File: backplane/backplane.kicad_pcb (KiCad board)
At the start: 2 copper layers, 150 x 150 mm, 16 parts

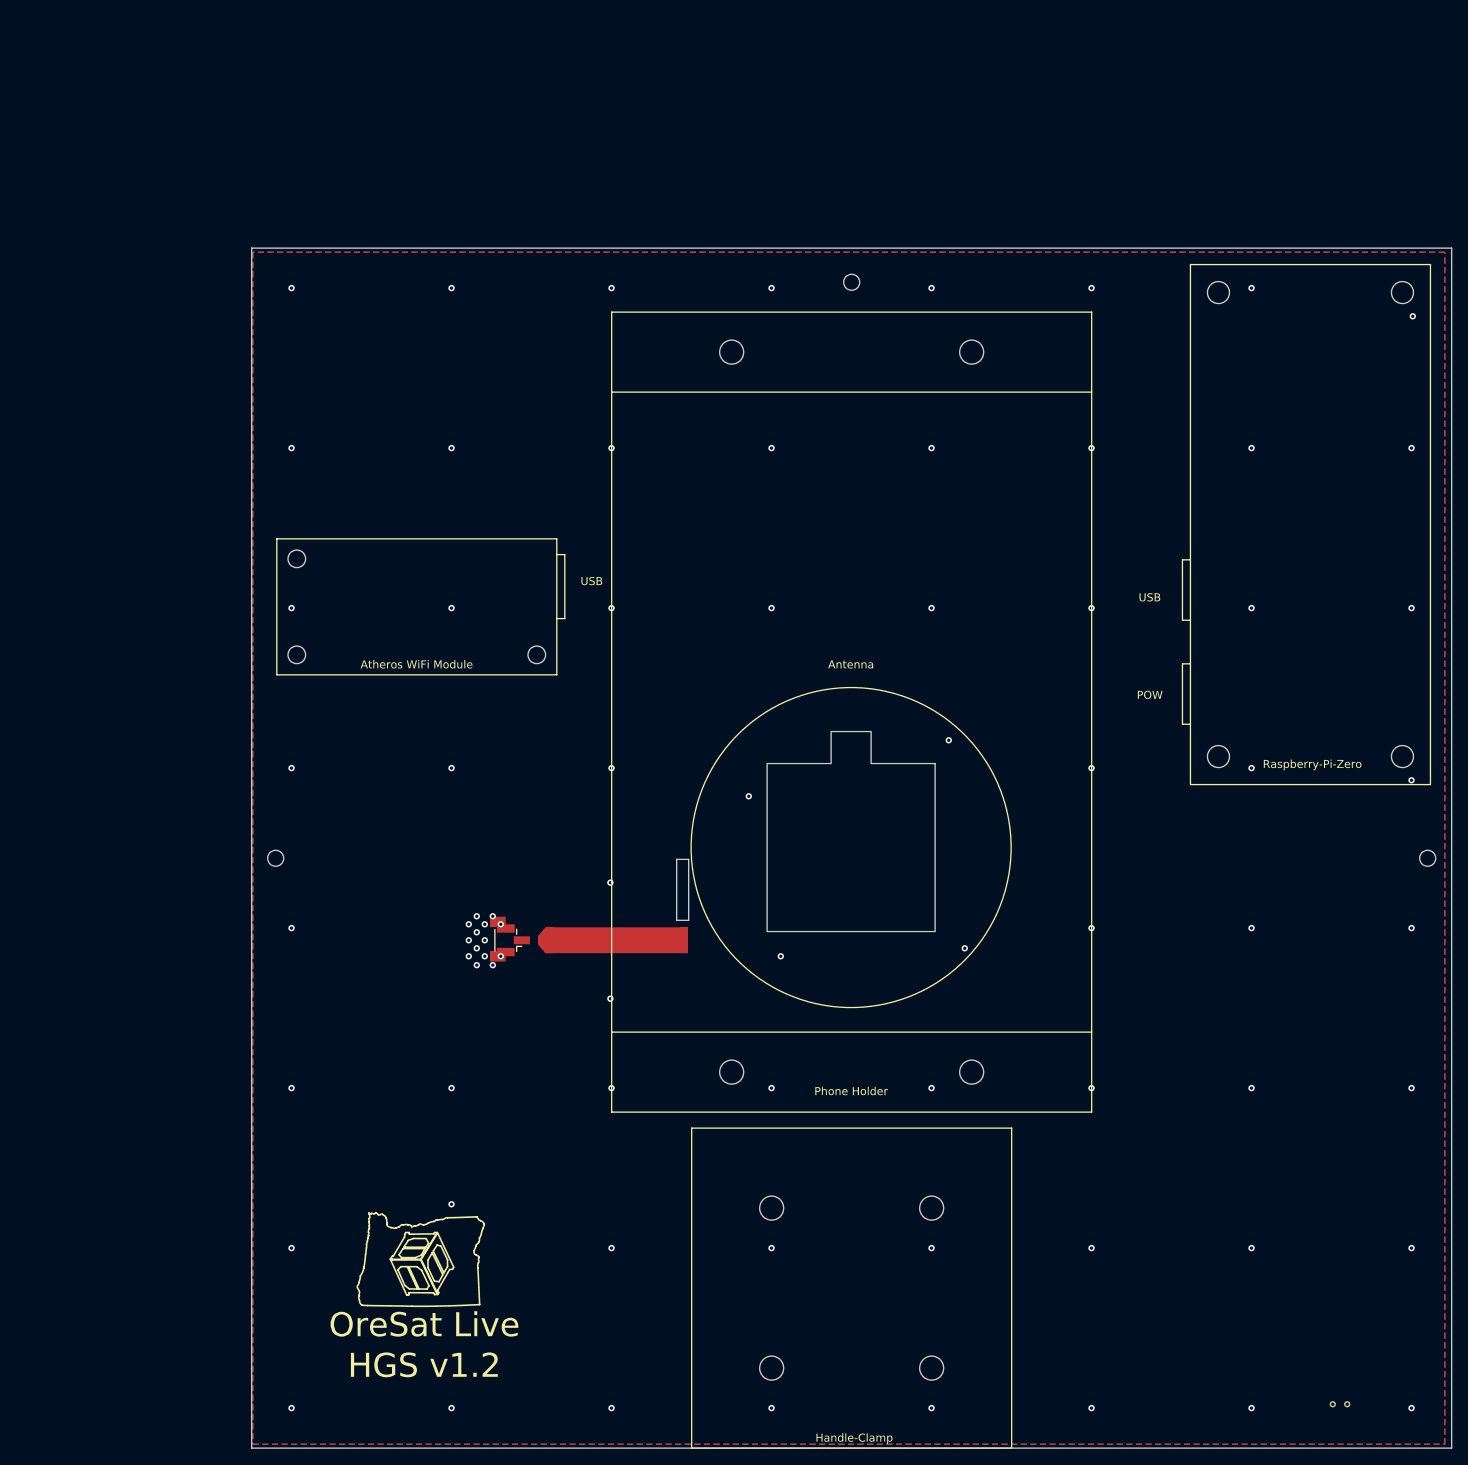
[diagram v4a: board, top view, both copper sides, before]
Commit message: Adding major final changes for transformer strip
Moved transformer parts closer to antenna by 1mm
Transformer microstrip reverted to original intended size
Added footprint for 0402 capacitor to replace gap between U.FL and strip
Modified U.FL footprint pads to be "solid" to allow for copper fill to
   connect to the GND pads
Phone Clamp and Handle mount holes changed to 4.5mm
Fixed README text hyperlink for footprint dimension references
Removed unused/blank footprints in Kicad library
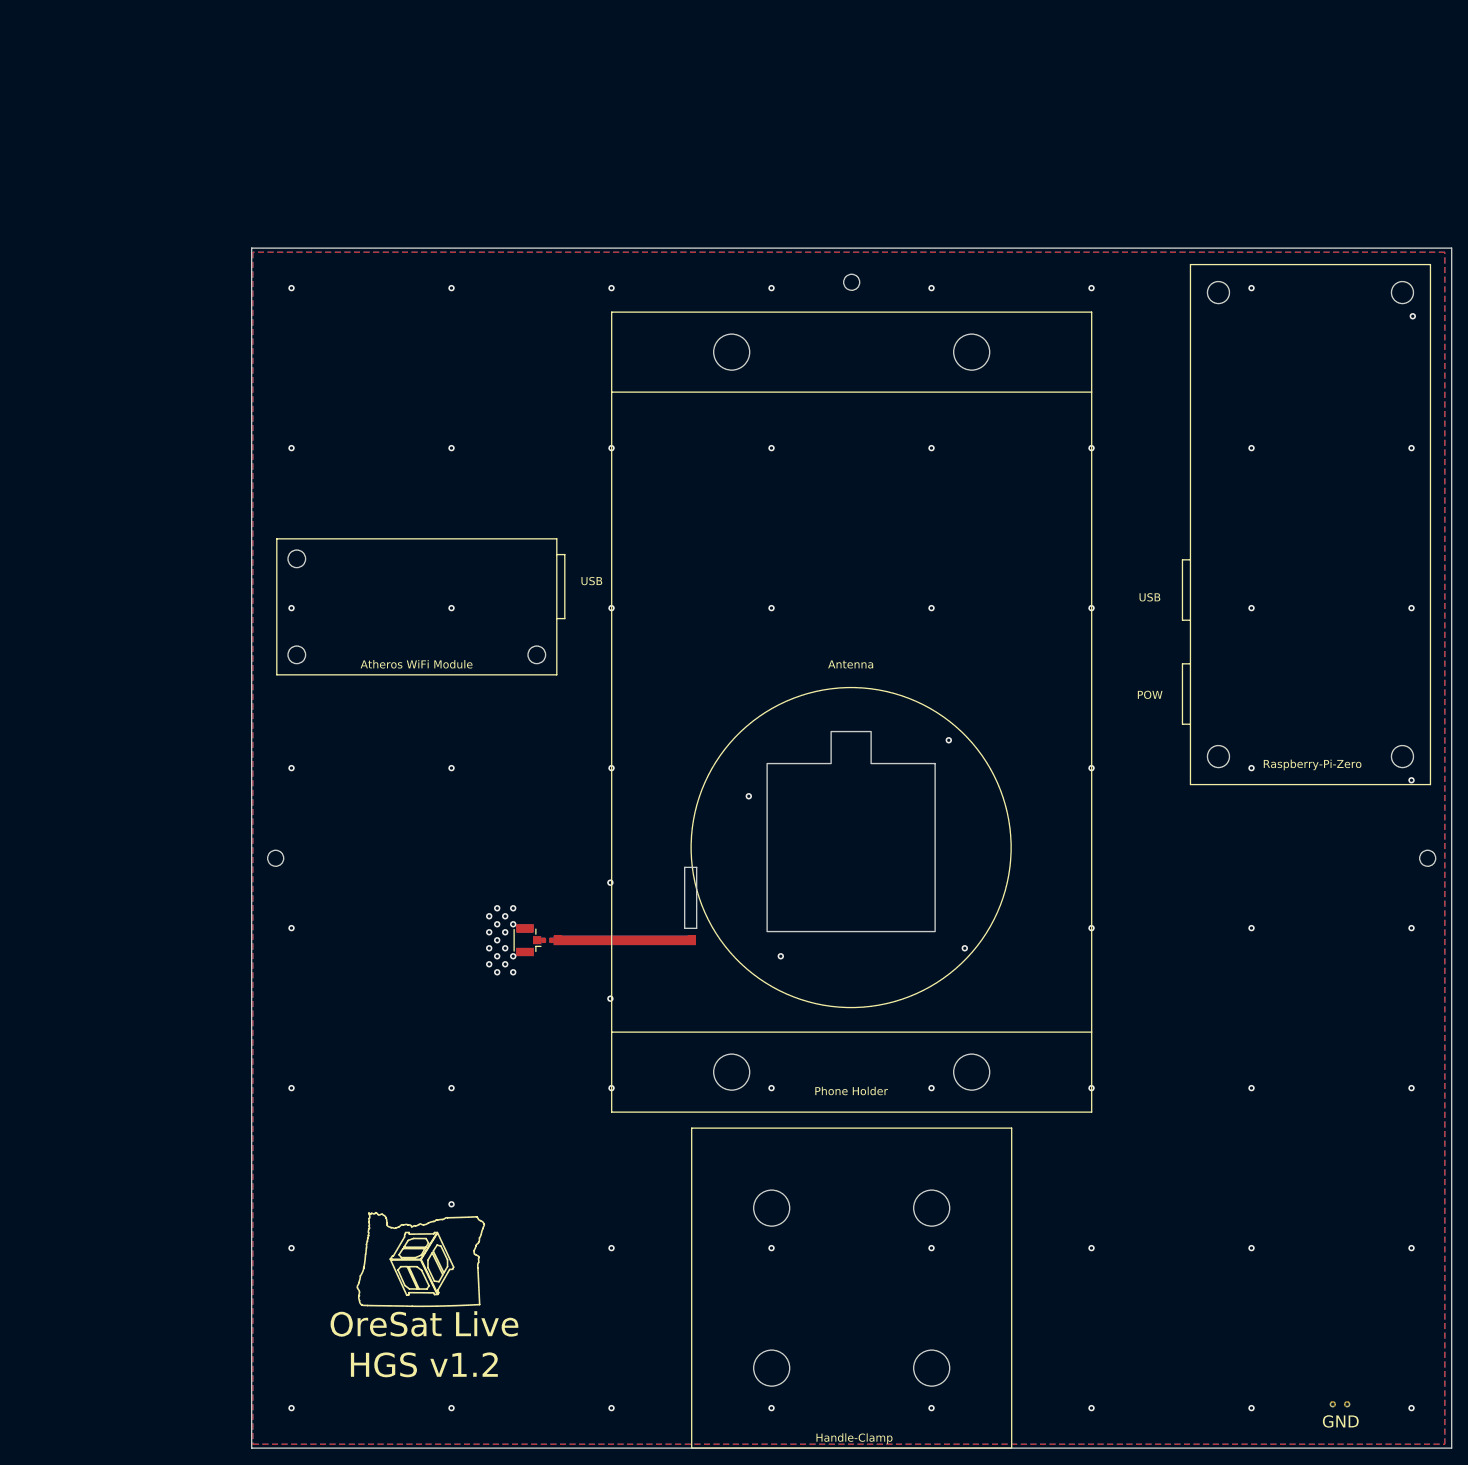
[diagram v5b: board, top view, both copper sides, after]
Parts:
- added REF**: C_0402_1005Metric, DxWiFi:C_0402_1005Metric, F.Cu at (59.9, 117.0)
- moved REF** 2.40 mm to (57.5, 117.0)
- moved REF** 1.41 mm to (79.8, 111.7)
- moved REF** 1.00 mm to (63.0, 117.0)
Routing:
- net Net-(L1-Pad1): vias 78 -> 81
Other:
- board text added: "GND"

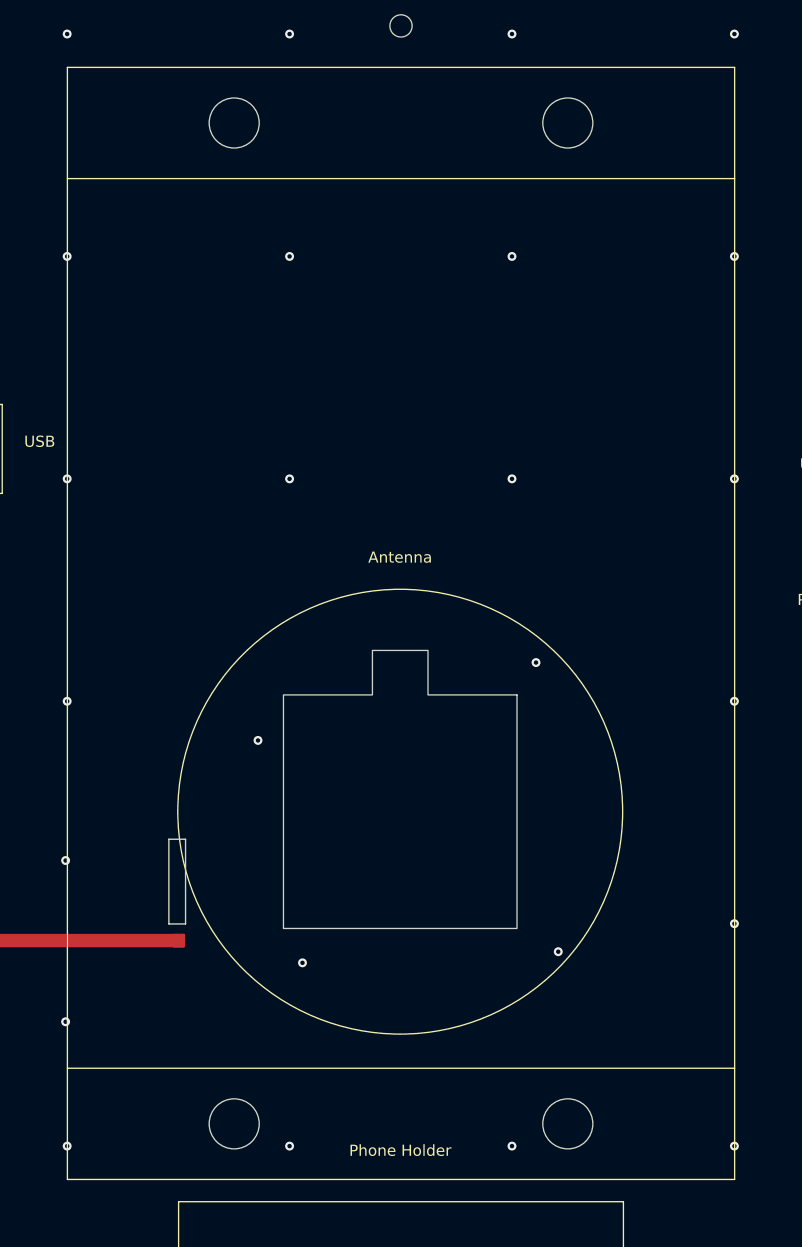
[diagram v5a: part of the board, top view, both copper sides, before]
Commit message: Update Phone Holder footprint to new design
Holes are now 50mm apart horizontally and 90mm vertically
Fixed hyperlinking text for README
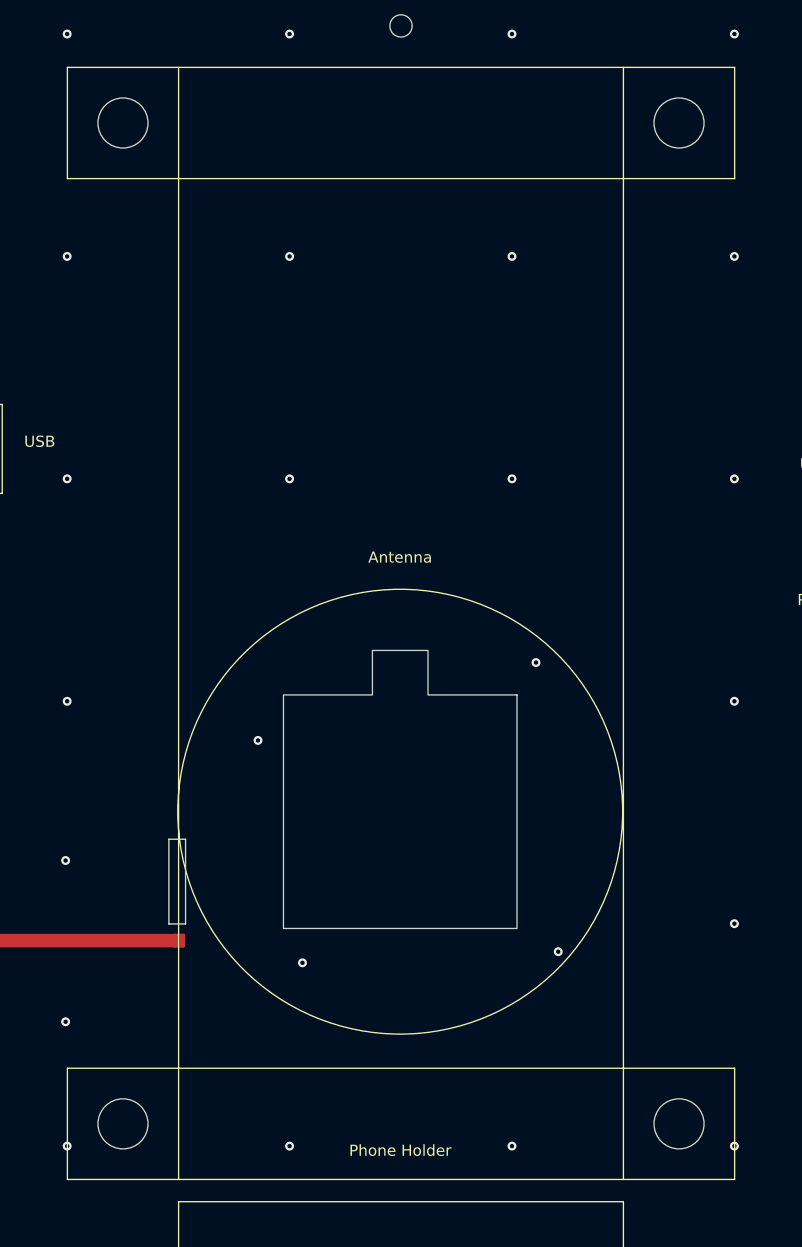
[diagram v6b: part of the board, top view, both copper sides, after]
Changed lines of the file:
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@@
     (add_net "Net-(L1-Pad1)")
+  )
+  (module DxWiFi:Phone-Holder (layer F.Cu)
+    (at 67.86 138.48)
+    (fp_text reference "Phone Holder" (at 29.93 -2.59) (layer F.SilkS)
+      (effects (font (size 1 1) (thickness 0.15)))
+    )
+    (fp_text value Phone-Holder (at 30.48 -5.13) (layer B.SilkS) hide
+      (effects (font (size 1 1) (thickness 0.15)))
+    )
+    (fp_line (start 60 -10) (end 60 0) (layer F.SilkS) (width 0.12))
+    (fp_line (start 0 -10) (end 0 0) (layer F.SilkS) (width 0.12))
+    (fp_line (start 60 -100) (end 60 -90) (layer F.SilkS) (width 0.12))
+    (fp_line (start 0 -100) (end 0 -90) (layer F.SilkS) (width 0.12))
+    (fp_line (start 0 -90) (end 60 -90) (layer F.SilkS) (width 0.12))
+    (fp_line (start 0 -10) (end 60 -10) (layer F.SilkS) (width 0.12))
+    (fp_line (start 10 -100) (end 10 0) (layer F.SilkS) (width 0.12))
+    (fp_line (start 0 -100) (end 60 -100) (layer F.SilkS) (width 0.12))
+    (fp_line (start 50 0) (end 50 -100) (layer F.SilkS) (width 0.12))
+    (fp_line (start 0 0) (end 60 0) (layer F.SilkS) (width 0.12))
+    (pad "" np_thru_hole circle (at 5 -95) (size 4.5 4.5) (drill 4.5) (layers *.Cu))
+    (pad "" np_thru_hole circle (at 55 -95) (size 4.5 4.5) (drill 4.5) (layers *.Cu))
+    (pad "" np_thru_hole circle (at 55 -5) (size 4.5 4.5) (drill 4.5) (layers *.Cu))
+    (pad "" np_thru_hole circle (at 5 -5) (size 4.5 4.5) (drill 4.5) (layers *.Cu))
   )
   (module DxWiFi:GND-pad (layer F.Cu)
@@
     (pad "" np_thru_hole circle (at 10 -10) (size 4.5 4.5) (drill 4.5) (layers *.Cu))
   )
-  (module DxWiFi:Phone-Holder (layer F.Cu)
-    (at 67.86 138.48)
-    (fp_text reference "Phone Holder" (at 29.93 -2.59) (layer F.SilkS)
-      (effects (font (size 1 1) (thickness 0.15)))
-    )
-    (fp_text value Phone-Holder (at 30.48 -5.13) (layer B.SilkS) hide
-      (effects (font (size 1 1) (thickness 0.15)))
-    )
-    (fp_line (start 0 -90) (end 60 -90) (layer F.SilkS) (width 0.12))
-    (fp_line (start 0 -10) (end 60 -10) (layer F.SilkS) (width 0.12))
-    (fp_line (start 0 -100) (end 0 0) (layer F.SilkS) (width 0.12))
-    (fp_line (start 60 -100) (end 0 -100) (layer F.SilkS) (width 0.12))
-    (fp_line (start 60 0) (end 60 -100) (layer F.SilkS) (width 0.12))
-    (fp_line (start 0 0) (end 60 0) (layer F.SilkS) (width 0.12))
-    (pad "" np_thru_hole circle (at 15 -95) (size 4.5 4.5) (drill 4.5) (layers *.Cu))
-    (pad "" np_thru_hole circle (at 45 -95) (size 4.5 4.5) (drill 4.5) (layers *.Cu))
-    (pad "" np_thru_hole circle (at 45 -5) (size 4.5 4.5) (drill 4.5) (layers *.Cu))
-    (pad "" np_thru_hole circle (at 15 -5) (size 4.5 4.5) (drill 4.5) (layers *.Cu))
-  )
   (module DxWiFi:C_0402_1005Metric (layer F.Cu)
